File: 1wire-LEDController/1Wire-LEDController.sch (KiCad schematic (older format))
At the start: 14 parts, among them J1 RJ45, J2 RJ45, P1 CONN_02X05, P2 Power Enable, P6 CONN_01X04, U1 LP2950, U2 STM32F030R8, U3 G3MB_SSR

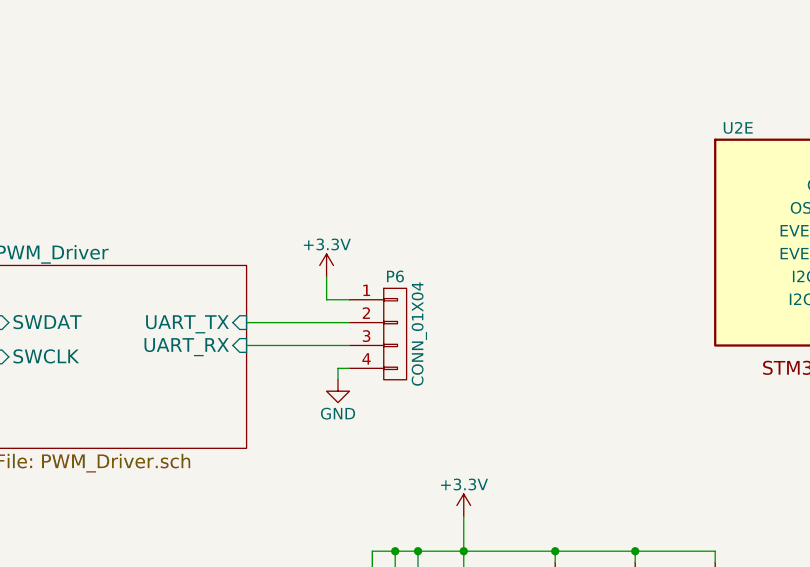
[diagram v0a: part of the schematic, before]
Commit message: 1Wire LED Controller Fix footprint of LP2950 voltage regulator Add a 1wire test point on the serial header
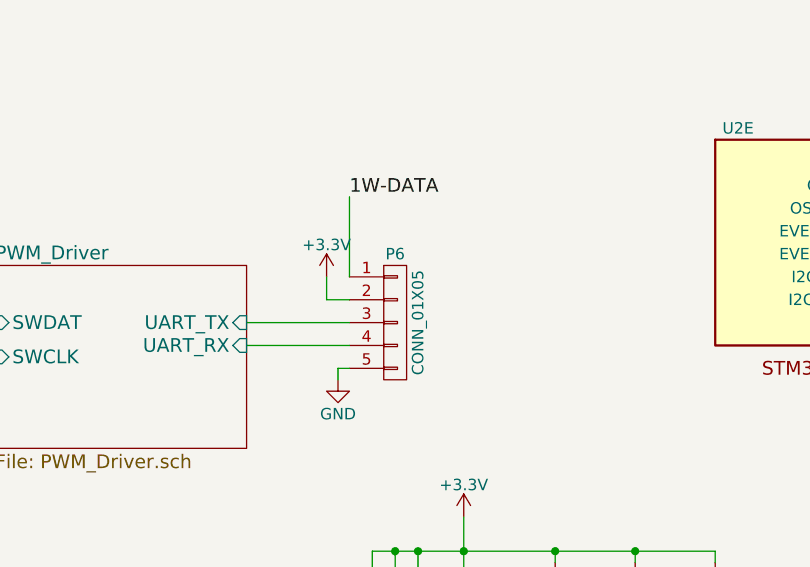
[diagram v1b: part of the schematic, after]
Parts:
- removed P6: CONN_01X04, Pin_Headers:Pin_Header_Straight_1x04, symbol CONN_01X04
- added P6: CONN_01X05, symbol CONN_01X05
- R1: footprint (none) -> Resistors_SMD:R_0603
- U1: footprint kicad-open-modules:D2PAK -> TO_SOT_Packages_SMD:TO-252-2Lead
- U2: footprint LQFP-64 -> Housings_QFP:LQFP-64_10x10mm_Pitch0.5mm
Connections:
- net +3V3: now also P6.2 (P2)
- net 1W-DATA: now also P6.1 (P1)
- net GND: now also P6.5 (P5)
- net PWM_Driver/UART_RX: now also P6.4 (P4)
- net PWM_Driver/UART_TX: now also P6.3 (P3)
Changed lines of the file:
@@
 $EndComp
 $Comp
-L GND #PWR4
+L GND #PWR01
 U 1 1 5824517A
 P 2650 2750
-F 0 "#PWR4" H 2650 2500 50  0001 C CNN
+F 0 "#PWR01" H 2650 2500 50  0001 C CNN
 F 1 "GND" H 2650 2600 50  0000 C CNN
 F 2 "" H 2650 2750 50  0000 C CNN
@@
 Connection ~ 2350 2400
 $Comp
-L +5V #PWR3
+L +5V #PWR02
 U 1 1 582452BF
 P 1550 2000
-F 0 "#PWR3" H 1550 1850 50  0001 C CNN
+F 0 "#PWR02" H 1550 1850 50  0001 C CNN
 F 1 "+5V" H 1550 2140 50  0000 C CNN
 F 2 "" H 1550 2000 50  0000 C CNN
@@
 	1550 2350 1550 2000
 $Comp
-L GND #PWR7
+L GND #PWR03
 U 1 1 58245334
 P 4500 7250
-F 0 "#PWR7" H 4500 7000 50  0001 C CNN
+F 0 "#PWR03" H 4500 7000 50  0001 C CNN
 F 1 "GND" H 4500 7100 50  0000 C CNN
 F 2 "" H 4500 7250 50  0000 C CNN
@@
 Connection ~ 4300 7050
 $Comp
-L +3.3V #PWR9
+L +3.3V #PWR04
 U 1 1 582453EE
 P 5050 5650
-F 0 "#PWR9" H 5050 5500 50  0001 C CNN
+F 0 "#PWR04" H 5050 5500 50  0001 C CNN
 F 1 "+3.3V" H 5050 5790 50  0000 C CNN
 F 2 "" H 5050 5650 50  0000 C CNN
@@
 	1900 4900 2700 4900
 $Comp
-L +3.3V #PWR1
+L +3.3V #PWR05
 U 1 1 582456BE
 P 1250 4700
-F 0 "#PWR1" H 1250 4550 50  0001 C CNN
+F 0 "#PWR05" H 1250 4550 50  0001 C CNN
 F 1 "+3.3V" H 1250 4840 50  0000 C CNN
 F 2 "" H 1250 4700 50  0000 C CNN
@@
 	1250 4800 1400 4800
 $Comp
-L GND #PWR2
+L GND #PWR06
 U 1 1 58245733
 P 1300 5300
-F 0 "#PWR2" H 1300 5050 50  0001 C CNN
+F 0 "#PWR06" H 1300 5050 50  0001 C CNN
 F 1 "GND" H 1300 5150 50  0000 C CNN
 F 2 "" H 1300 5300 50  0000 C CNN
@@
 F 0 "U1" H 5300 1354 60  0000 C CNN
 F 1 "LP2950" H 5150 1750 60  0000 C CNN
-F 2 "kicad-open-modules:D2PAK" H 5150 1550 60  0001 C CNN
+F 2 "TO_SOT_Packages_SMD:TO-252-2Lead" H 5150 1550 60  0001 C CNN
 F 3 "" H 5150 1550 60  0001 C CNN
 	1    5150 1550
@@
 $EndComp
 $Comp
-L GND #PWR10
+L GND #PWR07
 U 1 1 5825857A
 P 5150 1900
-F 0 "#PWR10" H 5150 1650 50  0001 C CNN
+F 0 "#PWR07" H 5150 1650 50  0001 C CNN
 F 1 "GND" H 5150 1750 50  0000 C CNN
 F 2 "" H 5150 1900 50  0000 C CNN
@@
 $EndComp
 $Comp
-L +5V #PWR8
+L +5V #PWR08
 U 1 1 5825859A
 P 4550 1100
-F 0 "#PWR8" H 4550 950 50  0001 C CNN
+F 0 "#PWR08" H 4550 950 50  0001 C CNN
 F 1 "+5V" H 4550 1240 50  0000 C CNN
 F 2 "" H 4550 1100 50  0000 C CNN
@@
 $EndComp
 $Comp
-L +3.3V #PWR12
+L +3.3V #PWR09
 U 1 1 582585BA
 P 5650 1400
-F 0 "#PWR12" H 5650 1250 50  0001 C CNN
+F 0 "#PWR09" H 5650 1250 50  0001 C CNN
 F 1 "+3.3V" H 5650 1540 50  0000 C CNN
 F 2 "" H 5650 1400 50  0000 C CNN
@@
 $EndComp
 $Comp
-L GND #PWR11
+L GND #PWR010
 U 1 1 58258D67
 P 5450 6250
-F 0 "#PWR11" H 5450 6000 50  0001 C CNN
+F 0 "#PWR010" H 5450 6000 50  0001 C CNN
 F 1 "GND" H 5450 6100 50  0000 C CNN
 F 2 "" H 5450 6250 50  0000 C CNN
@@
 	2850 2400 2850 1450
 $Comp
-L CONN_01X04 P6
-U 1 1 5827B051
-P 4750 4850
-F 0 "P6" H 4750 5100 50  0000 C CNN
-F 1 "CONN_01X04" V 4850 4850 50  0000 C CNN
-F 2 "Pin_Headers:Pin_Header_Straight_1x04" H 4750 4850 50  0001 C CNN
-F 3 "" H 4750 4850 50  0000 C CNN
-	1    4750 4850
-	1    0    0    -1
-$EndComp
-$Comp
-L +3.3V #PWR5
+L +3.3V #PWR011
 U 1 1 5827B1CE
 P 4450 4600
-F 0 "#PWR5" H 4450 4450 50  0001 C CNN
+F 0 "#PWR011" H 4450 4450 50  0001 C CNN
 F 1 "+3.3V" H 4450 4740 50  0000 C CNN
 F 2 "" H 4450 4600 50  0000 C CNN
@@
 	4450 4700 4450 4600
 $Comp
-L GND #PWR6
+L GND #PWR012
 U 1 1 5827B41B
 P 4500 5050
-F 0 "#PWR6" H 4500 4800 50  0001 C CNN
+F 0 "#PWR012" H 4500 4800 50  0001 C CNN
 F 1 "GND" H 4500 4900 50  0000 C CNN
 F 2 "" H 4500 5050 50  0000 C CNN
@@
 F 0 "U2" H 6250 4050 50  0000 C CNN
 F 1 "STM32F030R8" H 6450 4150 50  0001 C CNN
-F 2 "LQFP-64" H 6350 4250 50  0001 C CIN
+F 2 "Housings_QFP:LQFP-64_10x10mm_Pitch0.5mm" H 6350 4250 50  0001 C CIN
 F 3 "" H 9450 1500 50  0000 C CNN
 	5    6150 4000
@@
 	9150 4900 9150 5200
 $Comp
-L +5V #PWR13
+L +5V #PWR013
 U 1 1 58283957
 P 7850 4700
-F 0 "#PWR13" H 7850 4550 50  0001 C CNN
+F 0 "#PWR013" H 7850 4550 50  0001 C CNN
 F 1 "+5V" H 7850 4840 50  0000 C CNN
 F 2 "" H 7850 4700 50  0000 C CNN
@@
 F 0 "R1" V 4630 1250 50  0000 C CNN
 F 1 "33R" V 4550 1250 50  0000 C CNN
-F 2 "" V 4480 1250 50  0000 C CNN
+F 2 "Resistors_SMD:R_0603" V 4480 1250 50  0001 C CNN
 F 3 "" H 4550 1250 50  0000 C CNN
 	1    4550 1250
 	1    0    0    -1
 $EndComp
+$Comp
+L CONN_01X05 P6
+U 1 1 58B297A3
+P 4750 4800
+F 0 "P6" H 4750 5100 50  0000 C CNN
+F 1 "CONN_01X05" V 4850 4800 50  0000 C CNN
+F 2 "" H 4750 4800 50  0000 C CNN
+F 3 "" H 4750 4800 50  0000 C CNN
+	1    4750 4800
+	1    0    0    -1
+$EndComp
+Wire Wire Line
+	4550 4600 4550 4250
+Text Label 4550 4250 0    60   ~ 0
+1W-DATA
 $EndSCHEMATC

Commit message: Add 4 channel RGBW LED controller
Signed-off-by: Alastair D'Silva <alastair@d-silva.org>
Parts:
- removed P2: Power Enable, 2EDCK-Screw-Connectors:2EDCK-5.08-2PIN, symbol CONN_01X02
- removed U3: G3MB_SSR, SSR:G3MB, symbol G3MB_SSR
- added CON1: BARREL_JACK, Connect:BARREL_JACK, symbol BARREL_JACK
- added J3: JACK_STEREO, w_conn_av:jack_3.5_pj313d-smt, symbol JACK_STEREO
- added P2, P3, P5, P7: CONN_01X05, 2EDCK-Screw-Connectors:2EDCK-5.08-5PIN, symbol CONN_01X05
- added P4: DC_IN, 2EDCK-Screw-Connectors:2EDCK-5.08-2PIN, symbol CONN_01X02
- added Q1, Q10, Q11, Q12, Q13, Q14, Q15, Q16, Q2, Q3, Q4, Q5, Q6, Q7, Q8, Q9: IRLZ44NS, kicad-open-modules:D2PAK, symbol Q_NMOS_GDS
- added unit 3 of U2
- added unit 1 of U2
- P6: footprint (none) -> Pin_Headers:Pin_Header_Straight_1x05_Pitch2.54mm
- U2: footprint Housings_QFP:LQFP-64_10x10mm_Pitch0.5mm -> LQFP-64
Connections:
- net +5V: now also J3.1
- net 1W-DATA: now also U2.5 (OSC_IN/PF0); no longer U2.28 (PB2)
- net GND: now also CON1.2, CON1.3, J3.3, P4.1 (P1), Q1.3 (S), Q10.3 (S), Q11.3 (S), Q12.3 (S), Q13.3 (S), Q14.3 (S), Q15.3 (S), Q16.3 (S), Q2.3 (S), Q3.3 (S), Q4.3 (S), Q5.3 (S), Q6.3 (S), Q7.3 (S), Q8.3 (S), Q9.3 (S)
- net CHAN3_B: now reaches U2.27 (ADC1_IN9/TIM3_CH4/TIM14_CH1/TIM1_CH3N/PB1)
- net CHAN3_B: now also Q11.1 (G)
- net CHAN3_W: now reaches U2.29 (I2C2_SCL/PB10)
- net CHAN3_W: now also Q9.1 (G)
- net CHAN2_G: now reaches U2.33 (SPI2_NSS/TIM1_BKIN/EVENTOUT/PB12)
- net CHAN2_G: now also Q6.1 (G)
- net CHAN2_R: now reaches U2.34 (SPI2_SCK/I2C2_SDA/TIM1_CH1N/PB13)
- net CHAN2_R: now also Q4.1 (G)
- net CHAN2_B: now reaches U2.36 (SPI2_MOSI/TIM1_CH3N/TIM15_CH1N/TIM15_CH2/PB15)
- net CHAN2_B: now also Q2.1 (G)
- net CHAN0_R: now reaches U2.55 (SPI1_SCK/EVENTOUT/PB3)
- net CHAN0_R: now also Q14.1 (G)
- net CHAN0_B: now reaches U2.57 (SPI1_MOSI/I2C1_SMBA/TIM16_BKIN/TIM3_CH2/PB5)
- net CHAN0_B: now also Q12.1 (G)
- net CHAN0_W: now reaches U2.59 (I2C1_SDA/USART1_RX/TIM17_CH1N/PB7)
- net CHAN0_W: now also Q10.1 (G)
- net CHAN1_W: now reaches U2.48 (I2C2_SDA/PF8)
- net CHAN1_W: now also Q3.1 (G)
- net PWM_Driver/SWCLK renamed SWCLK
- net SWCLK: now also U2.49 (USART2_TX/SWCLK/PA14)
- net PWM_Driver/SWDAT renamed SWDAT
- net SWDAT: now also U2.46 (IR_OUT/SWDAT/PA13)
- net PWM_Driver/UART_RX renamed UART_RX
- net UART_RX: now also U2.17 (ADC1_IN3/USART2_RX/TIM15_CH2/PA3)
- net PWM_Driver/UART_TX renamed UART_TX
- net UART_TX: now also U2.16 (ADC1_IN2/USART2_TX/TIM15_CH1/PA2)
- new net: P3.1 (P1), Q1.2 (D)
- new net: P3.2 (P2), Q2.2 (D)
- new net: P3.3 (P3), Q4.2 (D)
- new net: P3.4 (P4), Q6.2 (D)
- new net: P7.1 (P1), Q10.2 (D)
- new net: P7.2 (P2), Q12.2 (D)
- new net: P7.3 (P3), Q14.2 (D)
- new net: P7.4 (P4), Q16.2 (D)
- new net: P5.1 (P1), Q3.2 (D)
- new net: P5.2 (P2), Q5.2 (D)
- new net: P5.3 (P3), Q7.2 (D)
- new net: P5.4 (P4), Q8.2 (D)
- new net: P2.1 (P1), Q9.2 (D)
- new net: P2.2 (P2), Q11.2 (D)
- new net: P2.3 (P3), Q13.2 (D)
- new net: P2.4 (P4), Q15.2 (D)
- new net +48V: CON1.1, P2.5 (P5), P3.5 (P5), P4.2 (P2), P5.5 (P5), P7.5 (P5)
- new net CHAN0_G: Q16.1 (G), U2.53 (PC12)
- new net CHAN1_B: Q5.1 (G), U2.44 (USART1_CTS/TIM1_CH4/EVENTOUT/PA11)
- new net CHAN1_G: Q8.1 (G), U2.40 (TIM3_CH4/PC9)
- new net CHAN1_R: Q7.1 (G), U2.42 (USART1_TX/TIM1_CH2/TIM15_BKIN/PA9)
- new net CHAN2_W: Q1.1 (G), U2.38 (TIM3_CH2/PC7)
- new net CHAN3_G: Q15.1 (G), U2.23 (ADC_IN7/SPI1_MOSI/TIM3_CH2/TIM14_CH1/TIM1_CH1N/TIM17_CH1/EVENTOUT/PA7)
- new net CHAN3_R: Q13.1 (G), U2.25 (ADC_IN15/EVENTOUT/PC5)
- new net MAINS_ENABLE: J3.2, U2.10 (ADC_IN12/EVENTOUT/PC2)
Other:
- moved on the sheet: C1, C2, C3, C4, C5, J1, J2, P1, P6, R1, U1, U2D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
